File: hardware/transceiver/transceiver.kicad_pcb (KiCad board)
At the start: 4 copper layers, 33.3 x 47.8 mm, 39 parts, among them J1 Conn_01x02, J2 Conn_01x04, J3 Micro_SD_Card_Det_Hirose_DM3AT, J4 Conn_Coaxial_Small, SW1 Reset, SW2 Boot, U1 SX1262IMLTRT, U2 PE4259, U4 ESP32-S3-MINI-1, Y1 32MHz

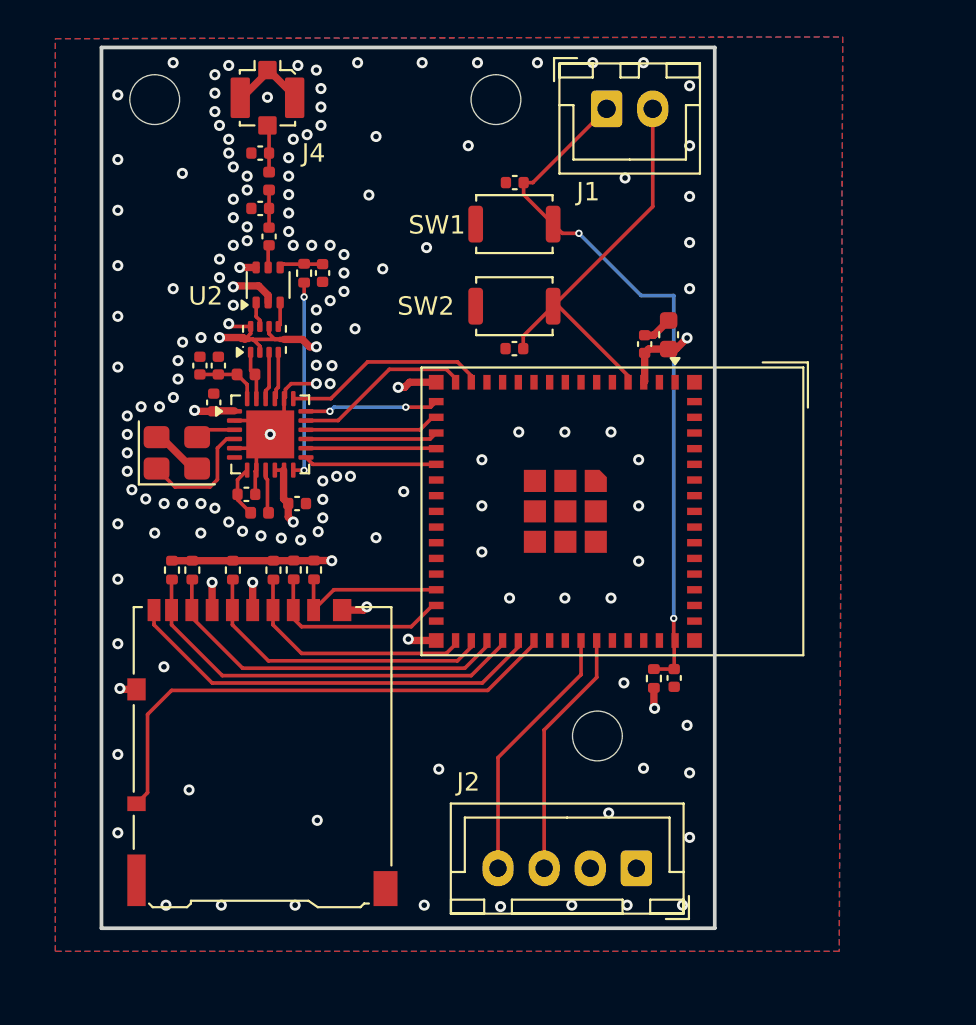
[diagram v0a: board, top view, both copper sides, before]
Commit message: redesigned tranceiver
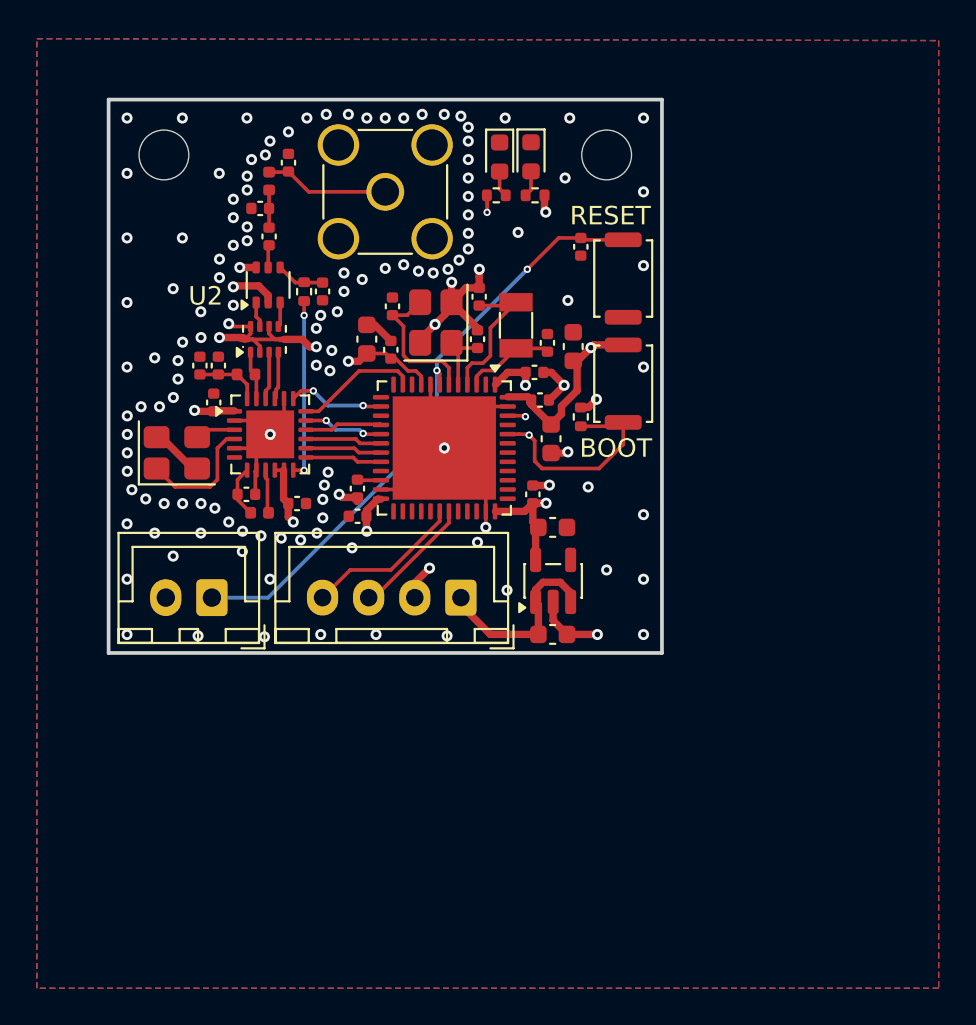
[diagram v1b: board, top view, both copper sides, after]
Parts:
- removed C11: 22uF, Capacitor_SMD:C_0603_1608Metric
- removed J4: Conn_Coaxial_Small, Connector_Coaxial:U.FL_Molex_MCRF_73412-0110_Vertical
- removed R10, R11, R12, R13, R14, R6, R9: 10K, Resistor_SMD:R_0402_1005Metric
- removed the REF** at (151.5, 128.5)
- removed the REF** at (146.0, 94.0)
- removed the REF** at (127.5, 94.0)
- removed SW2: Boot, Button_Switch_SMD:SW_Push_SPST_NO_Alps_SKRK
- added BOOT: Boot, Button_Switch_SMD:SW_Push_SPST_NO_Alps_SKRK, F.Cu at (152.9, 109.4)
- added C17: 0.1uF, Capacitor_SMD:C_0402_1005Metric, F.Cu at (148.1, 108.8)
- added C18: 0.1uF, Capacitor_SMD:C_0402_1005Metric, F.Cu at (148.0, 115.4)
- added C19: 1uF, Capacitor_SMD:C_0603_1608Metric, F.Cu at (139.0, 107.0)
- added C20: 1uF, Capacitor_SMD:C_0603_1608Metric, F.Cu at (150.2, 107.4)
- added C21: 0.1uF, Capacitor_SMD:C_0402_1005Metric, F.Cu at (140.3, 107.6)
- added C22: 10uF, Capacitor_SMD:C_0603_1608Metric, F.Cu at (149.0, 112.4)
- added C23: 4.7uF, Capacitor_SMD:C_0402_1005Metric, F.Cu at (138.5, 115.1)
- added C24: 8.2pF, Capacitor_SMD:C_0402_1005Metric, F.Cu at (140.4, 105.2)
- added C25: 15uF, Capacitor_SMD:C_0402_1005Metric, F.Cu at (148.8, 107.2)
- added C26: 15uF, Capacitor_SMD:C_0402_1005Metric, F.Cu at (145.1, 104.7)
- added C5: 1uF, Capacitor_SMD:C_0603_1608Metric, F.Cu at (149.1, 123.0)
- added C8: 1uF, Capacitor_SMD:C_0603_1608Metric, F.Cu at (149.1, 117.2)
- added D1: LED, LED_SMD:LED_0603_1608Metric, F.Cu at (146.2, 97.1)
- added D2: LED, LED_SMD:LED_0603_1608Metric, F.Cu at (147.9, 97.1)
- added R1: 10K, Resistor_SMD:R_0402_1005Metric, F.Cu at (150.6, 111.2)
- added R2: 1k, Resistor_SMD:R_0402_1005Metric, F.Cu at (148.1, 99.2)
- added R4: 1k, Resistor_SMD:R_0402_1005Metric, F.Cu at (146.0, 99.2)
- added REF**: MountingHole_2.7mm_M2.5, MountingHole:MountingHole_2.7mm_M2.5, F.Cu at (128.0, 97.0)
- added REF**: MountingHole_2.7mm_M2.5, MountingHole:MountingHole_2.7mm_M2.5, F.Cu at (152.0, 97.0)
- added U3: STM32U585CIUx, Package_DFN_QFN:QFN-48-1EP_7x7mm_P0.5mm_EP5.6x5.6mm, F.Cu at (143.2, 112.9)
- added Y2: Q13FC13500004, Crystal:Crystal_SMD_3215-2Pin_3.2x1.5mm, F.Cu at (147.1, 106.2)
- added Y3: X322516MLB4SI, Crystal:Crystal_SMD_3225-4Pin_3.2x2.5mm, F.Cu at (142.7, 106.1)
- C14: value 1uF -> 0.1uF
- C16: value 0.1uF -> 8.2pF
- J3: value Micro_SD_Card_Det_Hirose_DM3AT -> Conn_Coaxial; footprint Connector_Card:microSD_HC_Hirose_DM3AT-SF-PEJM5 -> Connector_Coaxial:SMA_Amphenol_901-144_Vertical
- U4: value ESP32-S3-MINI-1 -> AP2112K-3.3; footprint RF_Module:ESP32-S2-MINI-1 -> Package_TO_SOT_SMD:SOT-23-5
- moved J1 34.1 mm to (130.6, 121.0), turned to 180 degrees
- moved J3 31.1 mm to (140.0, 99.0)
- moved C12 18.1 mm to (138.5, 116.6), turned to 180 degrees
- moved J2 17.5 mm to (144.1, 121.0)
- moved C14 16.7 mm to (148.4, 110.3), turned to 0 degrees
- moved RESET 6.60 mm to (152.9, 103.7), turned to 90 degrees
- moved C15 4.99 mm to (150.6, 102.0), turned to 90 degrees
- moved U4 4.95 mm to (149.1, 120.1), turned to 90 degrees
- moved C16 2.06 mm to (145.0, 107.0), turned to 90 degrees
- moved C13 1.62 mm to (134.8, 97.4), turned to 90 degrees
- moved C7 1.00 mm to (136.6, 104.4)
- moved R3 1.00 mm to (135.6, 104.4)
- renumbered SW1 to RESET
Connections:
- C13 pad 1: Net-(J4-In) -> Net-(J3-In)
- C14 pad 1: GND -> +3.3V
- C14 pad 2: /EN -> GND
- C15 pad 2: /EN -> /RST
- C16 pad 1: GND -> /HSE_IN
- C16 pad 2: /BOOT -> GND
- J1 pad 1: /EN -> /RST
- J2 pad 1: +3.3V -> Net-(J2-Pin_1)
- J3 pad 1: /SD_DAT2 -> Net-(J3-In)
- J3 pad 2: /SD_DAT3 -> GND
- L3 pad 2: Net-(J4-In) -> Net-(J3-In)
- RESET pad 2: /EN -> /RST
- U4 pad 1: GND -> Net-(J2-Pin_1)
- U4 pad 3: +3.3V -> Net-(J2-Pin_1)
- U4 pad 4: /BOOT -> unconnected-(U4-NC-Pad4)
- U4 pad 5: unconnected-(U4-IO1-Pad5) -> +3.3V
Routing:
- net /EN: track 38.6 -> 0.00 mm, vias 2 -> 0
- net /RST: track 0.00 -> 33.5 mm, vias 0 -> 2
- net /SD_DET_0: track 27.8 -> 0.00 mm
- net GND: track 40.6 -> 64.9 mm, vias 148 -> 132
- net /SD_DET_1: track 23.0 -> 0.00 mm
- net /SD_DAT1: track 22.4 -> 0.00 mm
- net /SD_DAT0: track 20.0 -> 0.00 mm
- net /SD_CLK: track 16.9 -> 0.00 mm
- net Net-(U3-PB9): track 0.00 -> 13.8 mm, vias 0 -> 2
- net /SD_CMD: track 13.5 -> 0.00 mm
- net /BOOT: track 21.9 -> 35.2 mm, vias 0 -> 1
- net +3.3V: track 22.2 -> 34.9 mm, vias 7 -> 9
- net Net-(J2-Pin_1): track 0.00 -> 10.5 mm
- net /SD_DAT3: track 10.5 -> 0.00 mm
- net /SD_DAT2: track 8.78 -> 0.00 mm
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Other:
- board size 33.3 x 47.8 mm -> 30 x 30 mm

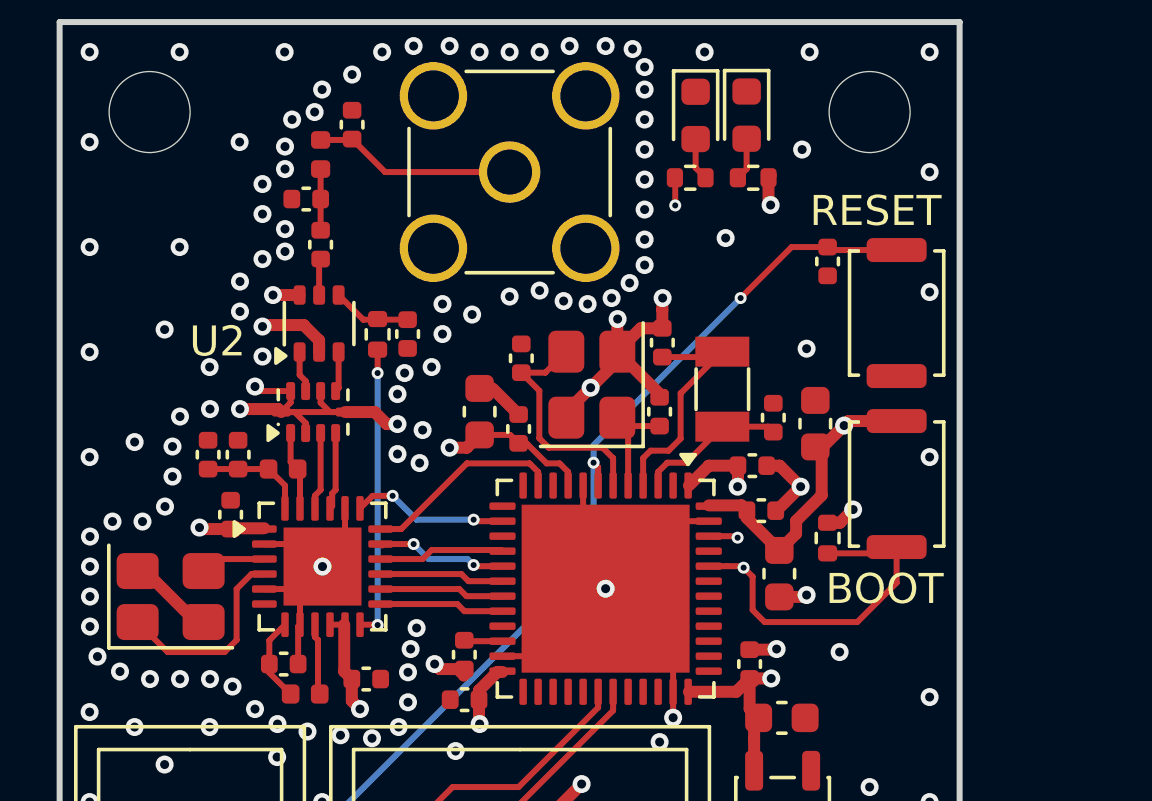
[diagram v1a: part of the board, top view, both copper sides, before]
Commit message: cleaning up transceiver
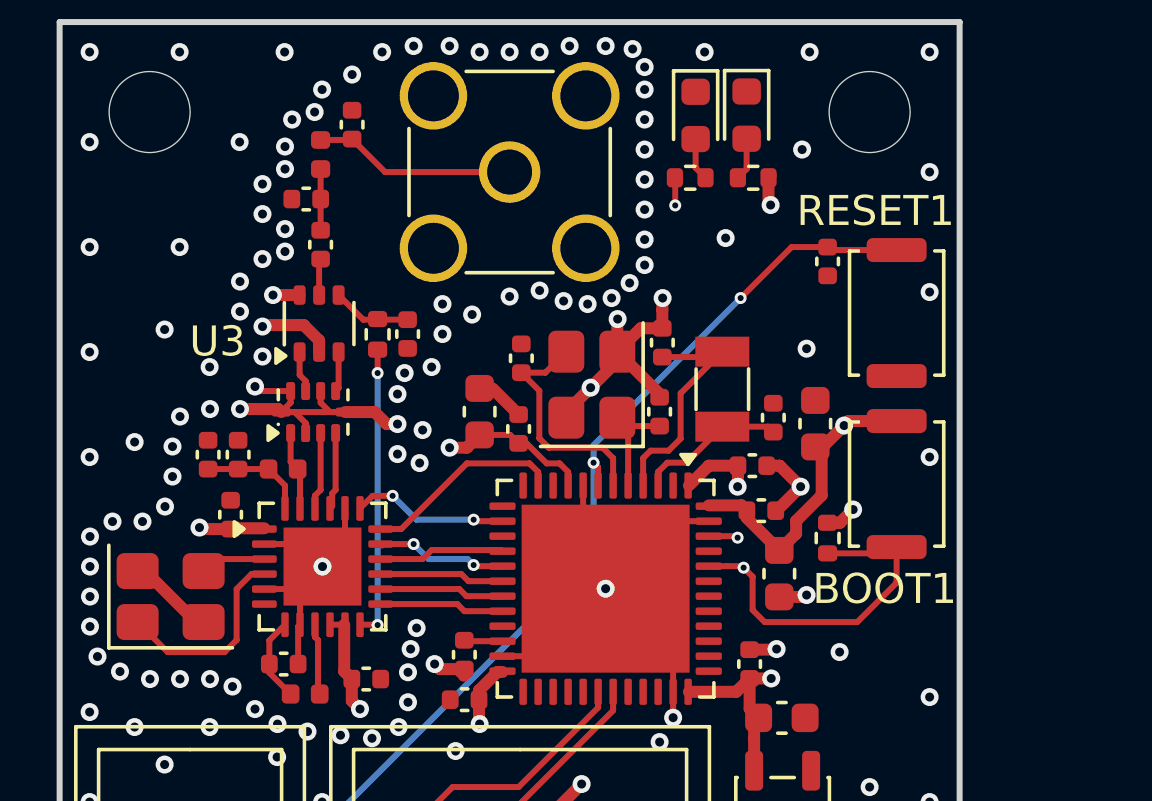
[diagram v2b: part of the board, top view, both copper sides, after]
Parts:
- renumbered BOOT to BOOT1, C13 to C11, C23 to C13, C17 to C15, C18 to C16, C21 to C17, C19 to C18, C20 to C19, C22 to C20, C15 to C21, C24 to C22, C25 to C23, C26 to C24, C16 to C25, C5 to C3, C3 to C4, C4 to C5, C8 to C7, C7 to C8, D2 to D1, D1 to D2, J2 to J1, J1 to J2, R3 to R1, R4 to R3, R1 to R4, RESET to RESET1, U4 to U2, U2 to U3, U3 to U4

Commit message: updated cad
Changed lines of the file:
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@@
 	)
 	(via
-		(at 141 102.95)
+		(at 140.85 103.1)
 		(size 0.6)
 		(drill 0.3)
@@
 	)
 	(via
-		(at 140 103.15)
+		(at 139.8 103.25)
 		(size 0.6)
 		(drill 0.3)
@@
 	)
 	(via
-		(at 137.7625 103.4)
+		(at 138.8 104.5)
 		(size 0.6)
 		(drill 0.3)
@@
 	)
 	(segment
-		(start 140.02 107.7625)
-		(end 140.3 108.0425)
+		(start 141.123703 108.6)
+		(end 141.65 108.6)
 		(width 0.2)
 		(layer "F.Cu")
@@
 	)
 	(segment
-		(start 141.664799 108.7115)
-		(end 141.95 108.996701)
-		(width 0.2)
-		(layer "F.Cu")
-		(net 3)
-	)
-	(segment
 		(start 148 115.88)
 		(end 147.555 116.325)
@@
 	)
 	(segment
-		(start 141.235203 108.7115)
-		(end 141.664799 108.7115)
+		(start 141.65 108.6)
+		(end 141.95 108.9)
+		(width 0.2)
+		(layer "F.Cu")
+		(net 3)
+	)
+	(segment
+		(start 140.3 108.0425)
+		(end 140.566203 108.0425)
 		(width 0.2)
 		(layer "F.Cu")
@@
 	)
 	(segment
-		(start 141.95 108.996701)
-		(end 141.95 109.45)
-		(width 0.2)
-		(layer "F.Cu")
-		(net 3)
-	)
-	(segment
 		(start 129.7125 110.9)
 		(end 130.7 110.9)
@@
 	)
 	(segment
-		(start 140.566203 108.0425)
-		(end 141.235203 108.7115)
-		(width 0.2)
+		(start 140.2075 107.95)
+		(end 140.3 108.0425)
+		(width 0.4)
 		(layer "F.Cu")
 		(net 3)
@@
 	)
 	(segment
-		(start 139 107.7625)
-		(end 140.02 107.7625)
-		(width 0.2)
-		(layer "F.Cu")
-		(net 3)
-	)
-	(segment
 		(start 147.555 116.325)
 		(end 145.976 116.325)
@@
 	)
 	(segment
-		(start 139.28 108.0425)
-		(end 139 107.7625)
-		(width 0.2)
-		(layer "F.Cu")
-		(net 3)
-	)
-	(segment
 		(start 147.609949 108.7875)
 		(end 146.6385 108.7875)
@@
 	)
 	(segment
+		(start 141.95 108.9)
+		(end 141.95 109.45)
+		(width 0.2)
+		(layer "F.Cu")
+		(net 3)
+	)
+	(segment
 		(start 147.909949 110.2875)
 		(end 147.909949 110.5325)
@@
 	)
 	(segment
+		(start 139.1875 107.95)
+		(end 140.2075 107.95)
+		(width 0.4)
+		(layer "F.Cu")
+		(net 3)
+	)
+	(segment
 		(start 134.74 115.9)
 		(end 134.4865 115.6465)
@@
 	)
 	(segment
-		(start 140.3 108.0425)
-		(end 140.566203 108.0425)
-		(width 0.2)
-		(layer "F.Cu")
-		(net 3)
-	)
-	(segment
 		(start 138.575 108.1875)
 		(end 139 107.7625)
@@
 	)
 	(segment
+		(start 140.566203 108.0425)
+		(end 141.123703 108.6)
+		(width 0.2)
+		(layer "F.Cu")
+		(net 3)
+	)
+	(segment
 		(start 138.98 116.5875)
 		(end 138.98 117.38)
@@
 		(start 147.909949 110.2875)
 		(end 147.733949 110.1115)
+		(width 0.4)
+		(layer "F.Cu")
+		(net 3)
+	)
+	(segment
+		(start 139 107.7625)
+		(end 139.1875 107.95)
 		(width 0.4)
 		(layer "F.Cu")
@@
 		(width 0.2)
 		(layer "F.Cu")
-		(net 22)
-	)
-	(segment
-		(start 135.749999 111.449999)
-		(end 135.7 111.4)
-		(width 0.2)
-		(layer "F.Cu")

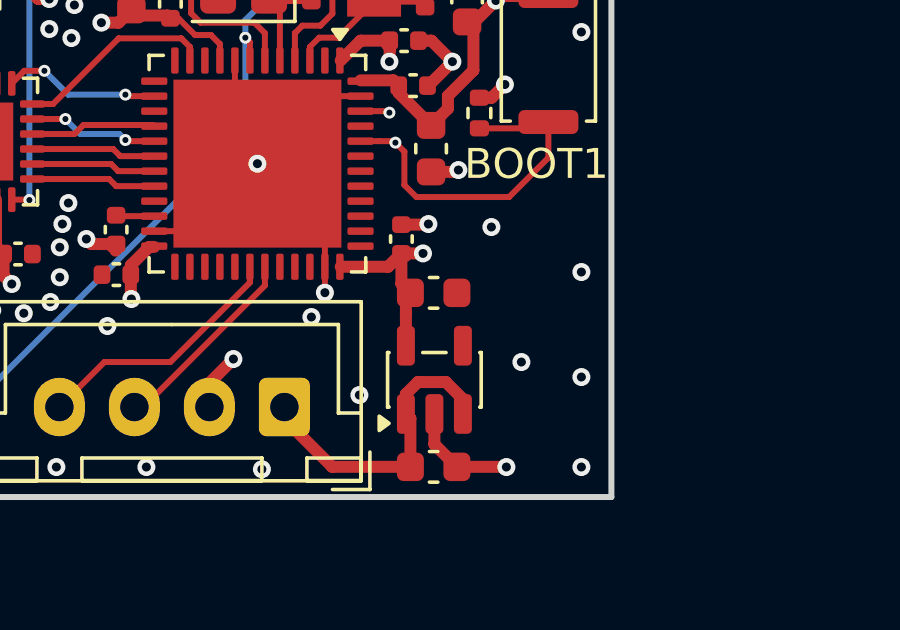
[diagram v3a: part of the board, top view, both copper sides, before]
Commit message: added SWD to transceiver
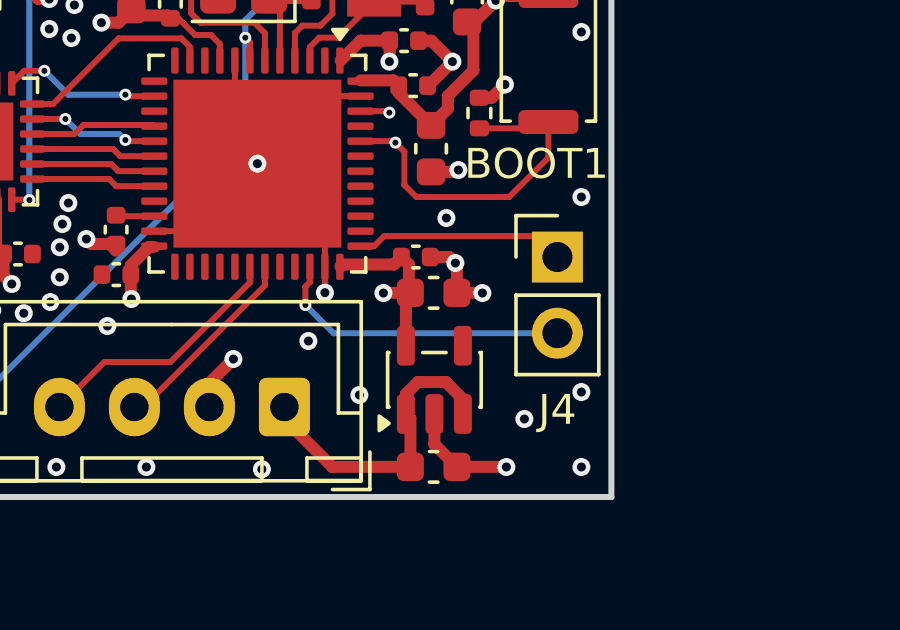
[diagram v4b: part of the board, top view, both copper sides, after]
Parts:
- added J4: Conn_01x02, Connector_PinHeader_2.54mm:PinHeader_1x02_P2.54mm_Vertical, F.Cu at (153.2, 116.0)
- moved C16 0.77 mm to (148.5, 116.0), turned to 0 degrees
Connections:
- U4 pad 34: unconnected-(U4-PA13-Pad34) -> /SWDIO
- U4 pad 37: unconnected-(U4-PA14-Pad37) -> /SWDCLK
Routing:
- net /SWDIO: track 0.00 -> 10.1 mm, vias 0 -> 1
- net /SWDCLK: track 0.00 -> 6.99 mm
- net GND: track 64.9 -> 66.8 mm, vias 132 -> 133

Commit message: added assets
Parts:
- renumbered BOOT1 to BOOT, RESET1 to RESET
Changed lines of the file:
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@@
 		(descr "http://www.alps.com/prod/info/E/HTML/Tact/SurfaceMount/SKRK/SKRKAHE020.html")
 		(tags "SMD SMT button")
-		(property "Reference" "RESET1"
+		(property "Reference" "RESET"
 			(at 3.4 -0.7 180)
 			(layer "F.SilkS")
@@
 		(descr "http://www.alps.com/prod/info/E/HTML/Tact/SurfaceMount/SKRK/SKRKAHE020.html")
 		(tags "SMD SMT button")
-		(property "Reference" "BOOT1"
+		(property "Reference" "BOOT"
 			(at 3.5 0.4 180)
 			(layer "F.SilkS")
@@
 		(polygon
 			(pts
-				(xy 121.1125 90.7) (xy 170 90.8) (xy 170 142.17375) (xy 121.1125 142.17375)
+				(xy 123.1125 92.7) (xy 156 92.8) (xy 156 126.17375) (xy 123.1125 126.17375)
 			)
 		)
@@
 		(polygon
 			(pts
-				(xy 122.1125 89.72375) (xy 171.8625 89.72375) (xy 171.8625 140.17375) (xy 122.1125 140.17375)
+				(xy 124.1125 91.72375) (xy 156.8625 91.72375) (xy 156.8625 125.17375) (xy 124.1125 125.17375)
 			)
 		)

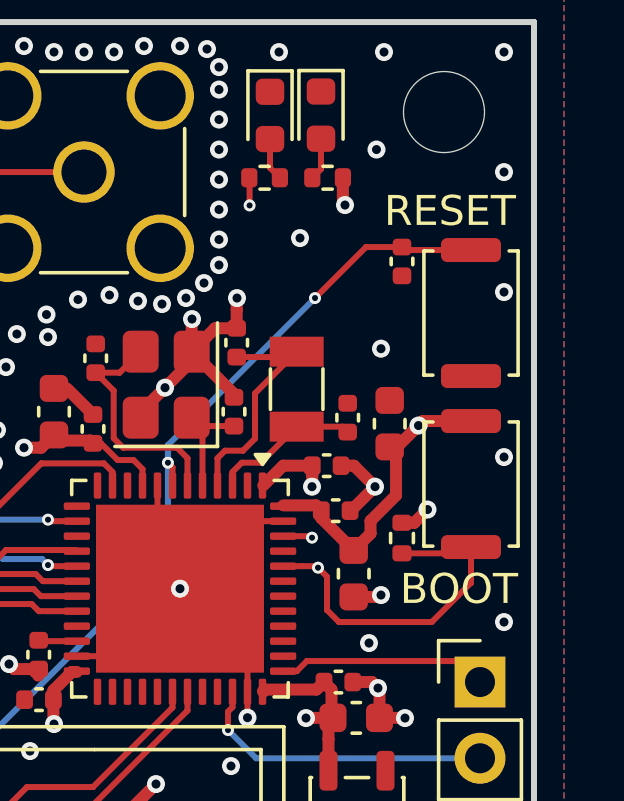
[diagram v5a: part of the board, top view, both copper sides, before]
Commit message: changed boot1 and reset1 to boot and reset
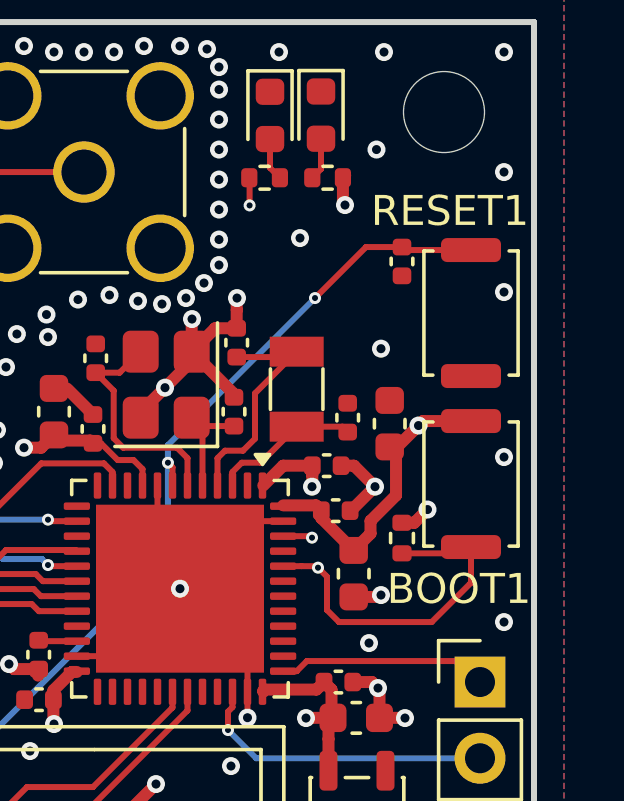
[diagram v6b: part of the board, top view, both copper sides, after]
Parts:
- renumbered BOOT to BOOT1, RESET to RESET1
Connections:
- net /IN_RX renamed /TX
- net /IN_TX renamed /RX
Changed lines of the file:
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@@
 	(net 12 "/SX_RFI_P")
 	(net 13 "/SX_RFO")
-	(net 14 "/IN_TX")
-	(net 15 "/IN_RX")
+	(net 14 "/RX")
+	(net 15 "/TX")
 	(net 16 "Net-(U1-DCC_SW)")
 	(net 17 "/SX_DIO2")
@@
 			(layers "*.Cu" "*.Mask")
 			(remove_unused_layers no)
-			(net 14 "/IN_TX")
+			(net 14 "/RX")
 			(pinfunction "Pin_3")
 			(pintype "passive")
@@
 			(layers "*.Cu" "*.Mask")
 			(remove_unused_layers no)
-			(net 15 "/IN_RX")
+			(net 15 "/TX")
 			(pinfunction "Pin_4")
 			(pintype "passive")
@@
 		(descr "http://www.alps.com/prod/info/E/HTML/Tact/SurfaceMount/SKRK/SKRKAHE020.html")
 		(tags "SMD SMT button")
-		(property "Reference" "RESET"
+		(property "Reference" "RESET1"
 			(at 3.4 -0.7 180)
 			(layer "F.SilkS")
@@
 			(layers "F.Cu" "F.Mask" "F.Paste")
 			(roundrect_rratio 0.25)
-			(net 15 "/IN_RX")
+			(net 15 "/TX")
 			(pinfunction "PA9")
 			(pintype "bidirectional")
@@
 			(layers "F.Cu" "F.Mask" "F.Paste")
 			(roundrect_rratio 0.25)
-			(net 14 "/IN_TX")
+			(net 14 "/RX")
 			(pinfunction "PA10")
 			(pintype "bidirectional")
@@
 		(descr "http://www.alps.com/prod/info/E/HTML/Tact/SurfaceMount/SKRK/SKRKAHE020.html")
 		(tags "SMD SMT button")
-		(property "Reference" "BOOT"
+		(property "Reference" "BOOT1"
 			(at 3.5 0.4 180)
 			(layer "F.SilkS")
